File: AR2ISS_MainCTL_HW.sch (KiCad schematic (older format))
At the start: 0 parts

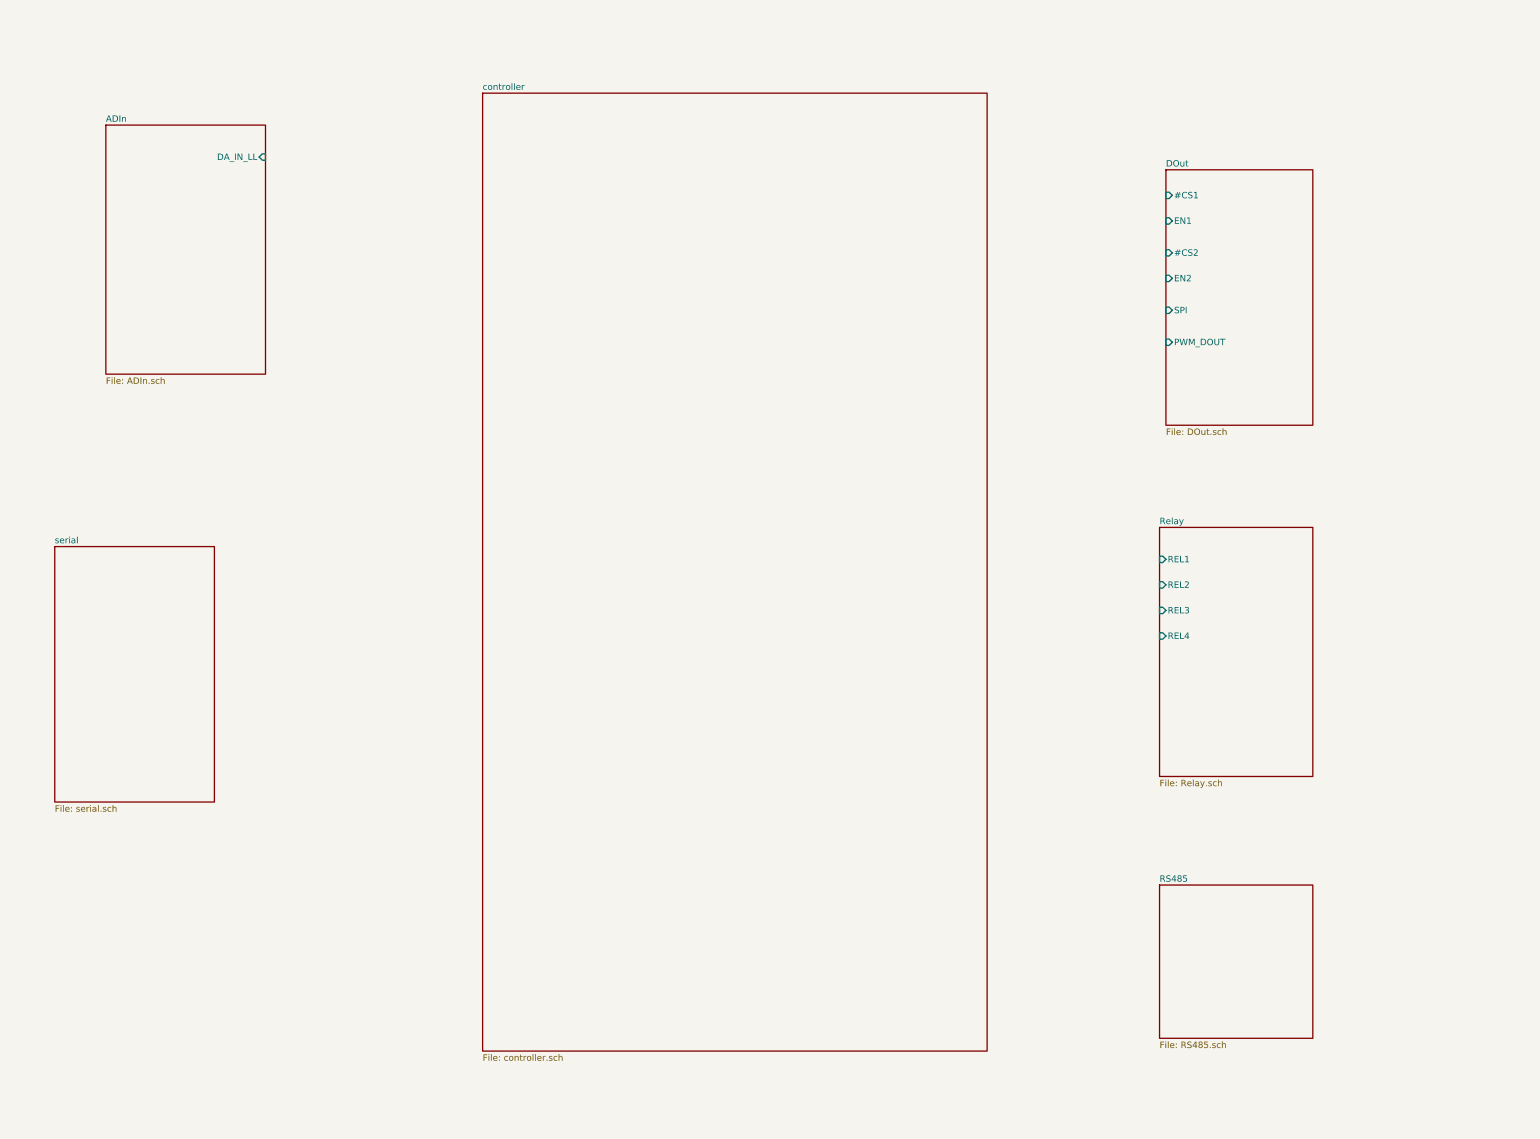
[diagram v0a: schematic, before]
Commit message: add RS422, RS232 filters
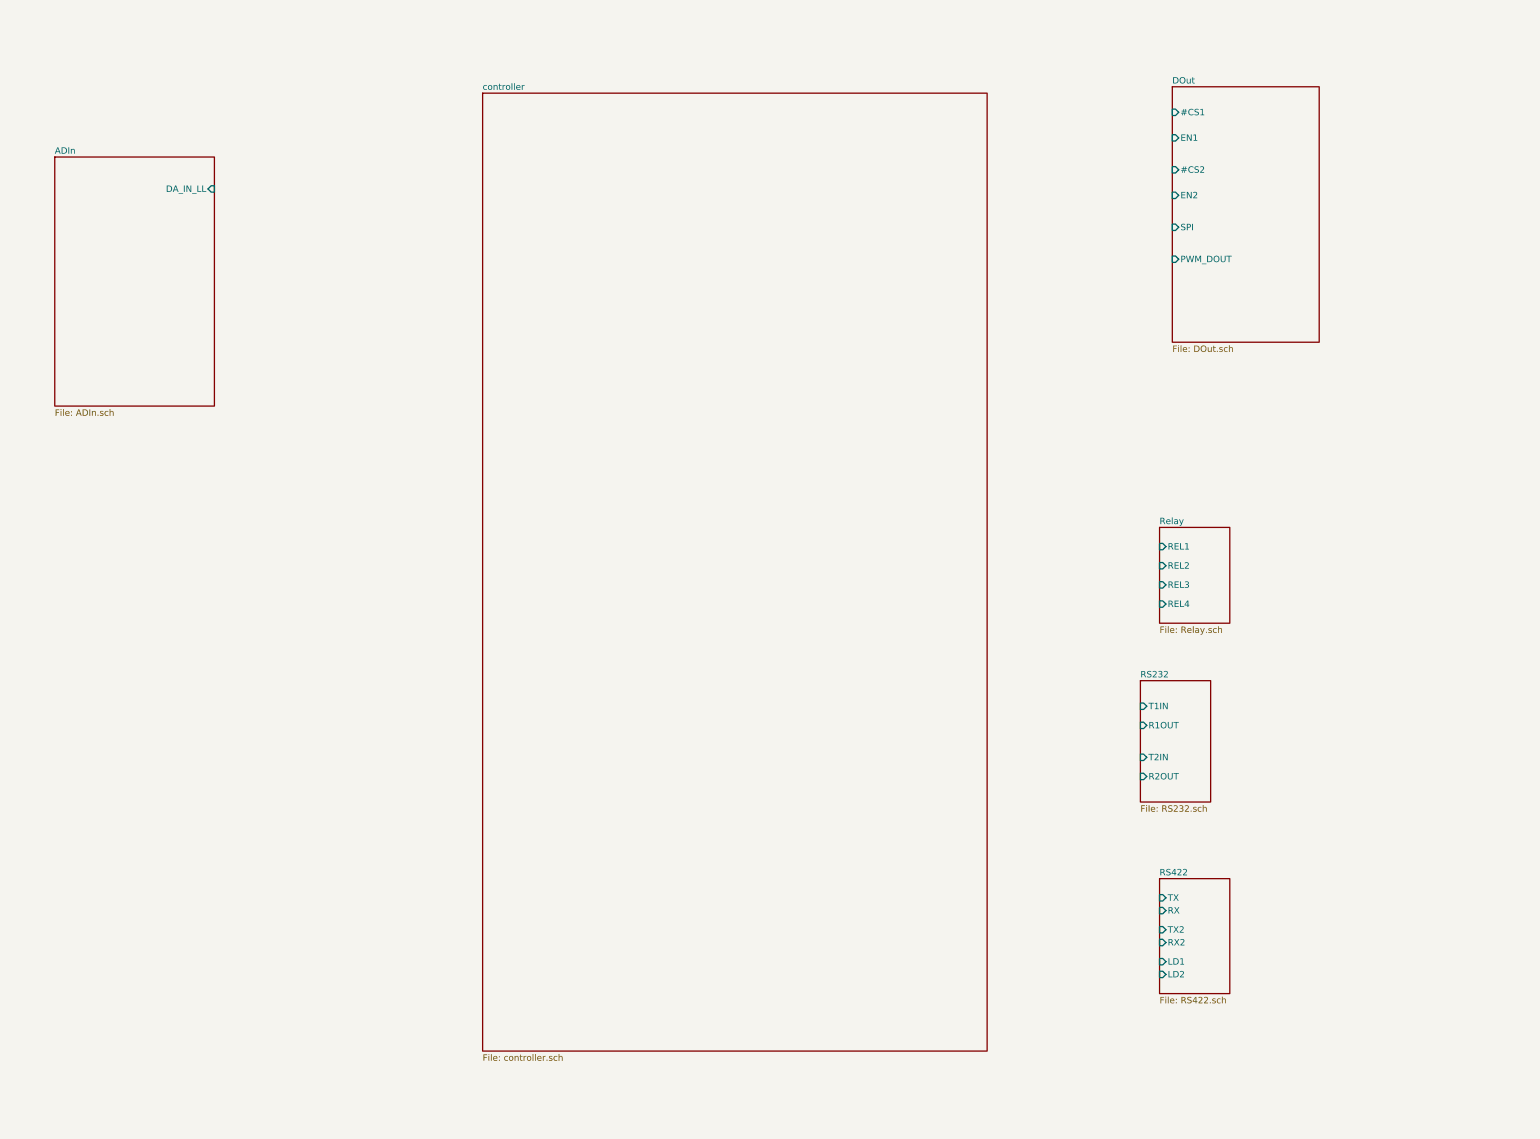
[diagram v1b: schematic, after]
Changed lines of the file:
@@
 $Descr A3 16535 11693
 encoding utf-8
-Sheet 1 7
+Sheet 1 10
 Title ""
 Date ""
@@
 $EndDescr
 $Sheet
-S 11300 5400 1200 1950
+S 11300 5400 550  750
 U 607A6028
 F0 "Relay" 50
 F1 "Relay.sch" 50
-F2 "REL1" I L 11300 5650 50
-F3 "REL2" I L 11300 5850 50
-F4 "REL3" I L 11300 6050 50
-F5 "REL4" I L 11300 6250 50
+F2 "REL1" I L 11300 5550 50
+F3 "REL2" I L 11300 5700 50
+F4 "REL3" I L 11300 5850 50
+F5 "REL4" I L 11300 6000 50
 $EndSheet
 $Sheet
-S 11350 2600 1150 2000
+S 11400 1950 1150 2000
 U 607BA83E
 F0 "DOut" 50
 F1 "DOut.sch" 50
-F2 "#CS1" I L 11350 2800 50
-F3 "EN1" I L 11350 3000 50
-F4 "#CS2" I L 11350 3250 50
-F5 "EN2" I L 11350 3450 50
-F6 "SPI" I L 11350 3700 50
-F7 "PWM_DOUT" I L 11350 3950 50
+F2 "#CS1" I L 11400 2150 50
+F3 "EN1" I L 11400 2350 50
+F4 "#CS2" I L 11400 2600 50
+F5 "EN2" I L 11400 2800 50
+F6 "SPI" I L 11400 3050 50
+F7 "PWM_DOUT" I L 11400 3300 50
 $EndSheet
 $Sheet
-S 3050 2250 1250 1950
+S 2650 2500 1250 1950
 U 6069F05D
 F0 "ADIn" 50
 F1 "ADIn.sch" 50
-F2 "DA_IN_LL" I R 4300 2500 50
+F2 "DA_IN_LL" I R 3900 2750 50
 $EndSheet
 $Sheet
@@
 $EndSheet
 $Sheet
-S 2650 5550 1250 2000
+S 11150 6600 550  950
 U 6089ADE2
-F0 "serial" 50
-F1 "serial.sch" 50
+F0 "RS232" 50
+F1 "RS232.sch" 50
+F2 "T1IN" I L 11150 6800 50
+F3 "T2IN" I L 11150 7200 50
+F4 "R1OUT" I L 11150 6950 50
+F5 "R2OUT" I L 11150 7350 50
 $EndSheet
 $Sheet
-S 11300 8200 1200 1200
+S 11300 8150 550  900
 U 608A378A
-F0 "RS485" 50
-F1 "RS485.sch" 50
+F0 "RS422" 50
+F1 "RS422.sch" 50
+F2 "TX" I L 11300 8300 50
+F3 "RX" I L 11300 8400 50
+F4 "TX2" I L 11300 8550 50
+F5 "RX2" I L 11300 8650 50
+F6 "LD1" I L 11300 8800 50
+F7 "LD2" I L 11300 8900 50
 $EndSheet
 $EndSCHEMATC

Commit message: add SDcard, OneWire, Batt, analog out, digital out
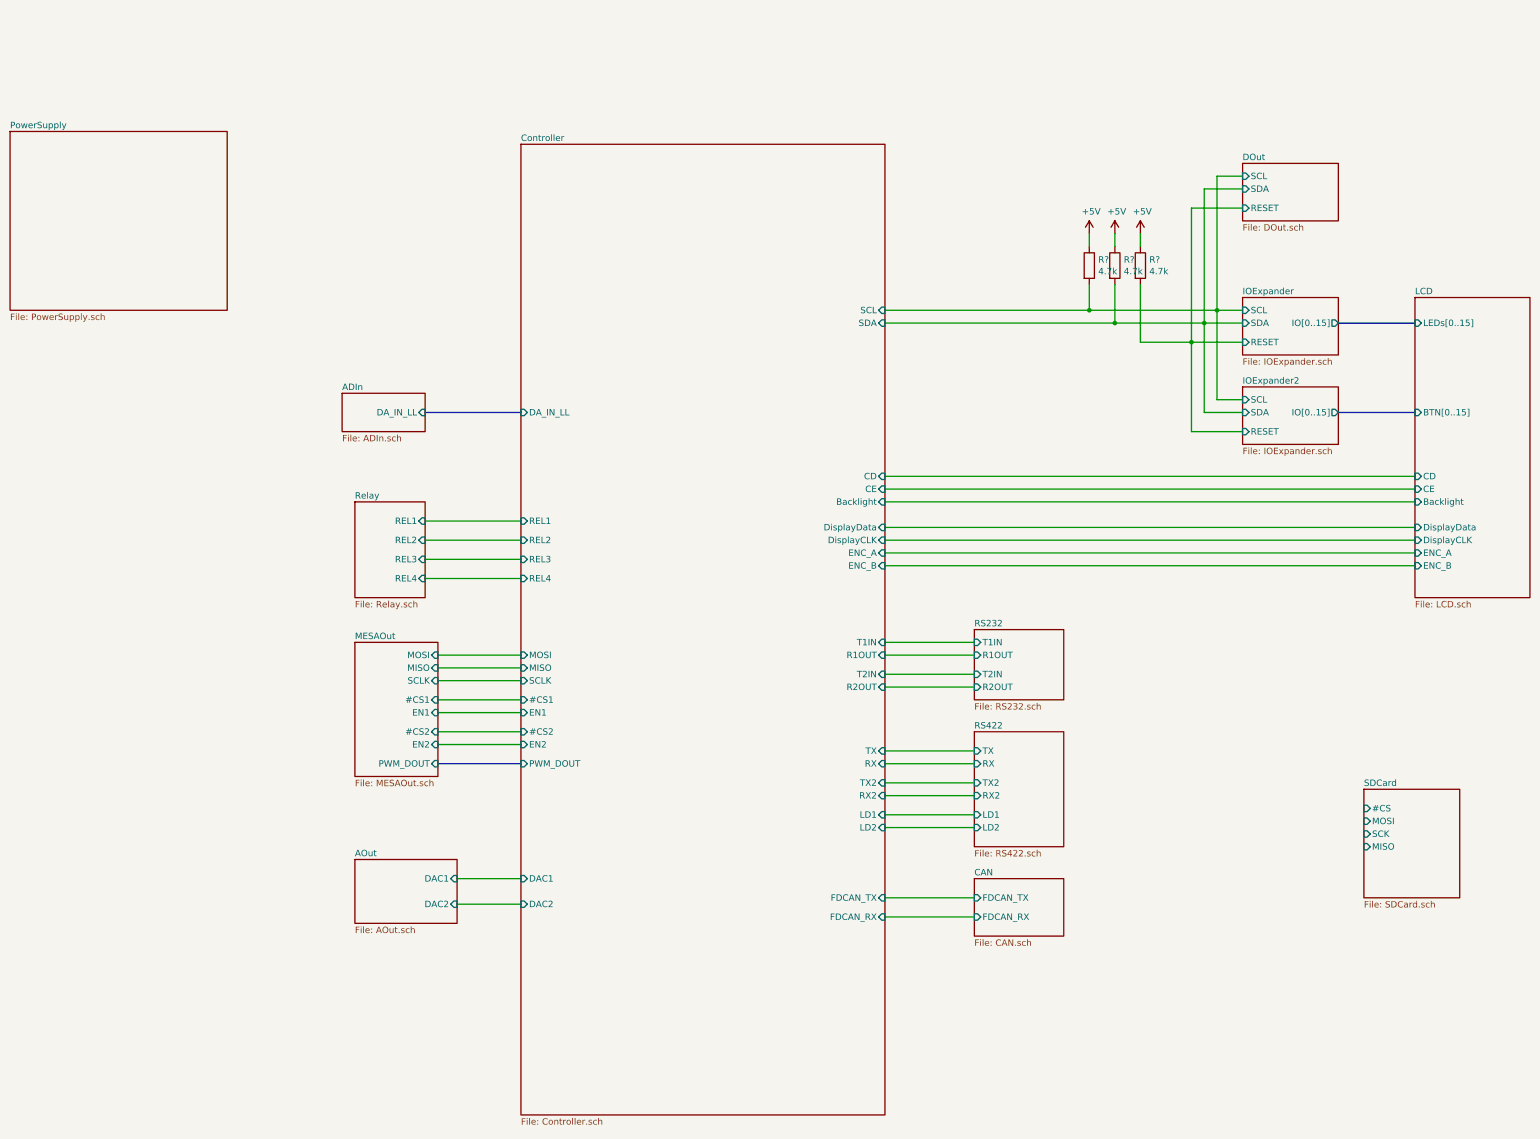
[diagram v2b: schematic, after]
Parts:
- added R? (x3): 4.7k, symbol AR2ISS:R
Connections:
- new net +5V: R?.1, R?.1, R?.1
- new net Controller/SCL: R?.2
- new net Controller/SDA: R?.2
- new net DOut/RESET: R?.2

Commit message: start placement
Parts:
- R1, R2, R3: renamed from R?; footprint (none) -> Resistor_SMD:R_0603_1608Metric
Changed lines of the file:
@@
 $Descr A3 16535 11693
 encoding utf-8
-Sheet 1 19
+Sheet 1 21
 Title ""
 Date ""
@@
 F4 "R1OUT" I L 9850 6400 50
 F5 "R2OUT" I L 9850 6650 50
-$EndSheet
-$Sheet
-S 9850 7000 700  900
-U 608A378A
-F0 "RS422" 50
-F1 "RS422.sch" 50
-F2 "TX" I L 9850 7150 50
-F3 "RX" I L 9850 7250 50
-F4 "TX2" I L 9850 7400 50
-F5 "RX2" I L 9850 7500 50
-F6 "LD1" I L 9850 7650 50
-F7 "LD2" I L 9850 7750 50
 $EndSheet
 $Sheet
@@
 	11550 3950 11950 3950
 $Comp
-L AR2ISS:R R?
+L AR2ISS:R R3
 U 1 1 60A2CA1D
 P 11150 3350
-F 0 "R?" H 11220 3396 50  0000 L CNN
+F 0 "R3" H 11220 3396 50  0000 L CNN
 F 1 "4.7k" H 11220 3305 50  0000 L CNN
-F 2 "" V 11080 3350 50  0001 C CNN
+F 2 "Resistor_SMD:R_0603_1608Metric" V 11080 3350 50  0001 C CNN
 F 3 "~" H 11150 3350 50  0001 C CNN
 	1    11150 3350
@@
 $EndComp
 $Comp
-L AR2ISS:R R?
+L AR2ISS:R R2
 U 1 1 60A2CE7F
 P 10950 3350
-F 0 "R?" H 11020 3396 50  0000 L CNN
+F 0 "R2" H 11020 3396 50  0000 L CNN
 F 1 "4.7k" H 11020 3305 50  0000 L CNN
-F 2 "" V 10880 3350 50  0001 C CNN
+F 2 "Resistor_SMD:R_0603_1608Metric" V 10880 3350 50  0001 C CNN
 F 3 "~" H 10950 3350 50  0001 C CNN
 	1    10950 3350
@@
 $EndComp
 $Comp
-L AR2ISS:R R?
+L AR2ISS:R R1
 U 1 1 60A2CFE6
 P 10750 3350
-F 0 "R?" H 10820 3396 50  0000 L CNN
+F 0 "R1" H 10820 3396 50  0000 L CNN
 F 1 "4.7k" H 10820 3305 50  0000 L CNN
-F 2 "" V 10680 3350 50  0001 C CNN
+F 2 "Resistor_SMD:R_0603_1608Metric" V 10680 3350 50  0001 C CNN
 F 3 "~" H 10750 3350 50  0001 C CNN
 	1    10750 3350
@@
 Connection ~ 10750 3700
 $Comp
-L power:+5V #PWR?
+L power:+5V #PWR03
 U 1 1 60A2D84C
 P 11150 3100
-F 0 "#PWR?" H 11150 2950 50  0001 C CNN
+F 0 "#PWR03" H 11150 2950 50  0001 C CNN
 F 1 "+5V" H 11165 3273 50  0000 C CNN
 F 2 "" H 11150 3100 50  0001 C CNN
@@
 $EndComp
 $Comp
-L power:+5V #PWR?
+L power:+5V #PWR02
 U 1 1 60A2DD5C
 P 10950 3100
-F 0 "#PWR?" H 10950 2950 50  0001 C CNN
+F 0 "#PWR02" H 10950 2950 50  0001 C CNN
 F 1 "+5V" H 10965 3273 50  0000 C CNN
 F 2 "" H 10950 3100 50  0001 C CNN
@@
 $EndComp
 $Comp
-L power:+5V #PWR?
+L power:+5V #PWR01
 U 1 1 60A2DF69
 P 10750 3100
-F 0 "#PWR?" H 10750 2950 50  0001 C CNN
+F 0 "#PWR01" H 10750 2950 50  0001 C CNN
 F 1 "+5V" H 10765 3273 50  0000 C CNN
 F 2 "" H 10750 3100 50  0001 C CNN
@@
 F36 "EN2" I L 6300 7100 50
 F37 "PWM_DOUT" I L 6300 7250 50
+F38 "SD_#CS" I R 9150 9150 50
+F39 "SD_MOSI" I R 9150 9250 50
+F40 "SD_MISO" I R 9150 9450 50
+F41 "SD_SCK" I R 9150 9350 50
 $EndSheet
 Wire Bus Line
@@
 	6300 5800 5550 5800
 $Sheet
-S 12900 7450 750  850
+S 9850 9000 750  850
 U 60B18BF8
 F0 "SDCard" 50
 F1 "SDCard.sch" 50
-F2 "#CS" I L 12900 7600 50
-F3 "MOSI" I L 12900 7700 50
-F4 "SCK" I L 12900 7800 50
-F5 "MISO" I L 12900 7900 50
+F2 "#CS" I L 9850 9150 50
+F3 "MOSI" I L 9850 9250 50
+F4 "SCK" I L 9850 9350 50
+F5 "MISO" I L 9850 9450 50
 $EndSheet
 $Sheet
@@
 Wire Wire Line
 	5650 6400 6300 6400
+Wire Wire Line
+	9150 9150 9850 9150
+Wire Wire Line
+	9850 9250 9150 9250
+Wire Wire Line
+	9150 9350 9850 9350
+Wire Wire Line
+	9850 9450 9150 9450
+$Sheet
+S 9850 7000 550  900
+U 608DA584
+F0 "RS422" 50
+F1 "RS422.sch" 50
+F2 "LD1" I L 9850 7650 50
+F3 "LD2" I L 9850 7750 50
+F4 "TX" I L 9850 7150 50
+F5 "PTT2" I L 9850 7500 50
+F6 "PTT1" I L 9850 7400 50
+F7 "RX" I L 9850 7250 50
+$EndSheet
 $EndSCHEMATC
